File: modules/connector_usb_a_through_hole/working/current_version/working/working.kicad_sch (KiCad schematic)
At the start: 1 part, among them J1 scuath

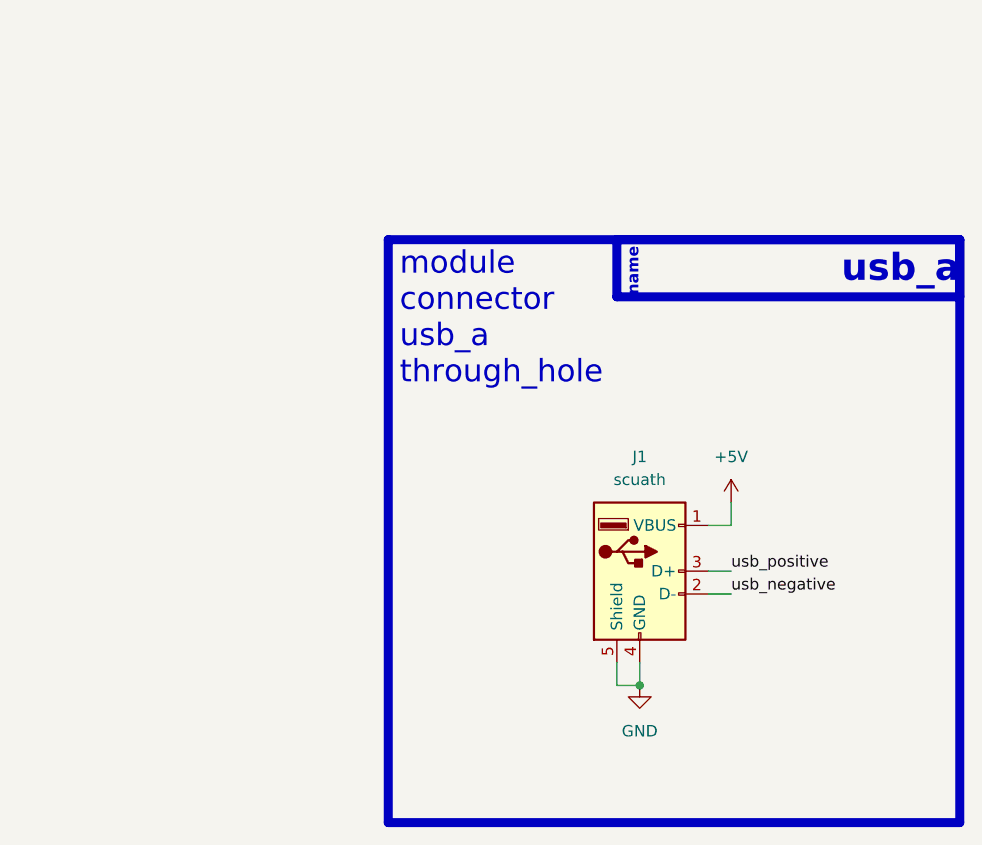
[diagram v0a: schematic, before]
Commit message: fixed formatting to be more consistent
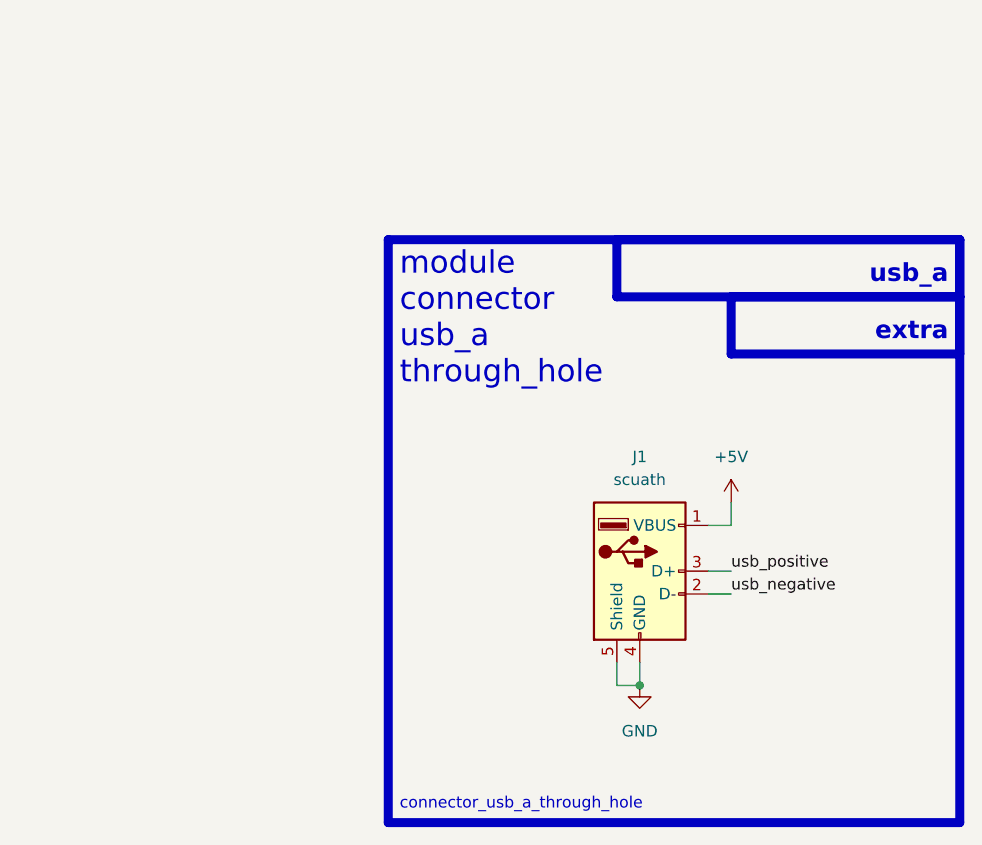
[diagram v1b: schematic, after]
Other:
- note added: "connector_usb_a_through_hole"
- note added: "extra"
- note removed: "name"
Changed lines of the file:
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@@
+    (fill (type none))
+  )
+  (rectangle (start 151.13 67.31) (end 176.53 73.66)
+    (stroke (width 1) (type default))
     (fill (type none))
   )
   (rectangle (start 138.43 60.96) (end 176.53 67.31)
     (stroke (width 1) (type default))
-    (fill (type color) (color 0 0 0 0))
+    (fill (type none))
   )
   (text "module\nconnector\nusb_a\nthrough_hole\n\n" (at 114.3 81.28 0)
     (effects (font (size 2.5 2.5)) (justify left bottom))
   )
-  (text "name" (at 140.97 67.31 90)
-    (effects (font (size 1.27 1.27) (thickness 0.254) bold (color 255 255 255 1)) (justify left bottom))
+  (text "connector_usb_a_through_hole" (at 114.3 124.46 0)
+    (effects (font (size 1.27 1.27)) (justify left bottom))
   )
-  (text "usb_a" (at 176.53 66.04 0)
-    (effects (font (size 3 3) (thickness 0.8) bold (color 255 255 255 1)) (justify right bottom))
+  (text "extra" (at 175.26 72.39 0)
+    (effects (font (size 2 2) (thickness 0.8) bold) (justify right bottom))
+  )
+  (text "usb_a" (at 175.26 66.04 0)
+    (effects (font (size 2 2) (thickness 0.8) bold) (justify right bottom))
   )
   (label "usb_positive" (at 151.13 97.79 0) (fields_autoplaced)

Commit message: a few fix ups
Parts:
- renumbered J1 to CON1
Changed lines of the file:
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@@
   (symbol (lib_id "oomlout_oomp_part_symbols:scuath_electronic_socket_usb_a_through_hole") (at 140.97 97.79 0) (unit 1)
     (in_bom yes) (on_board yes) (dnp no) (fields_autoplaced)
-    (property "Reference" "J1" (at 140.97 85.09 0)
+    (property "Reference" "CON1" (at 140.97 85.09 0)
       (effects (font (size 1.27 1.27)))
     )
@@
       (project "working"
         (path "/c9993764-076f-44f6-bf4c-6b69ce17c9e4"
-          (reference "J1") (unit 1)
+          (reference "CON1") (unit 1)
         )
       )

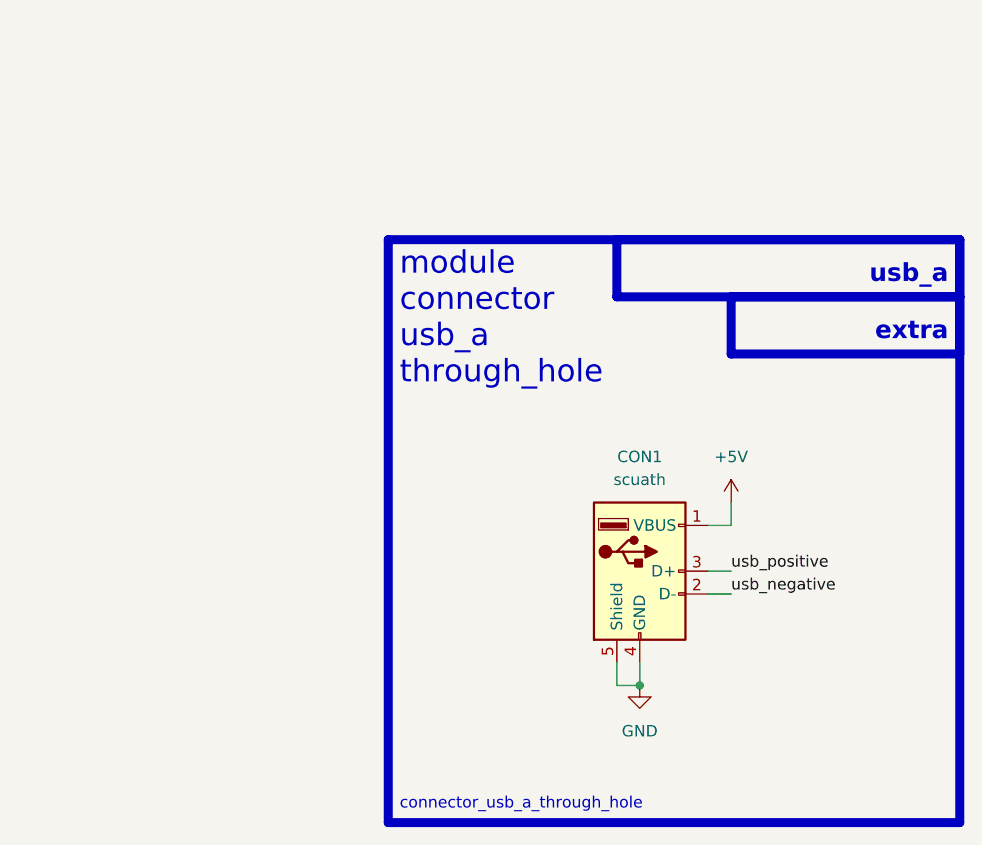
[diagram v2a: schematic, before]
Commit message: schematic formatting
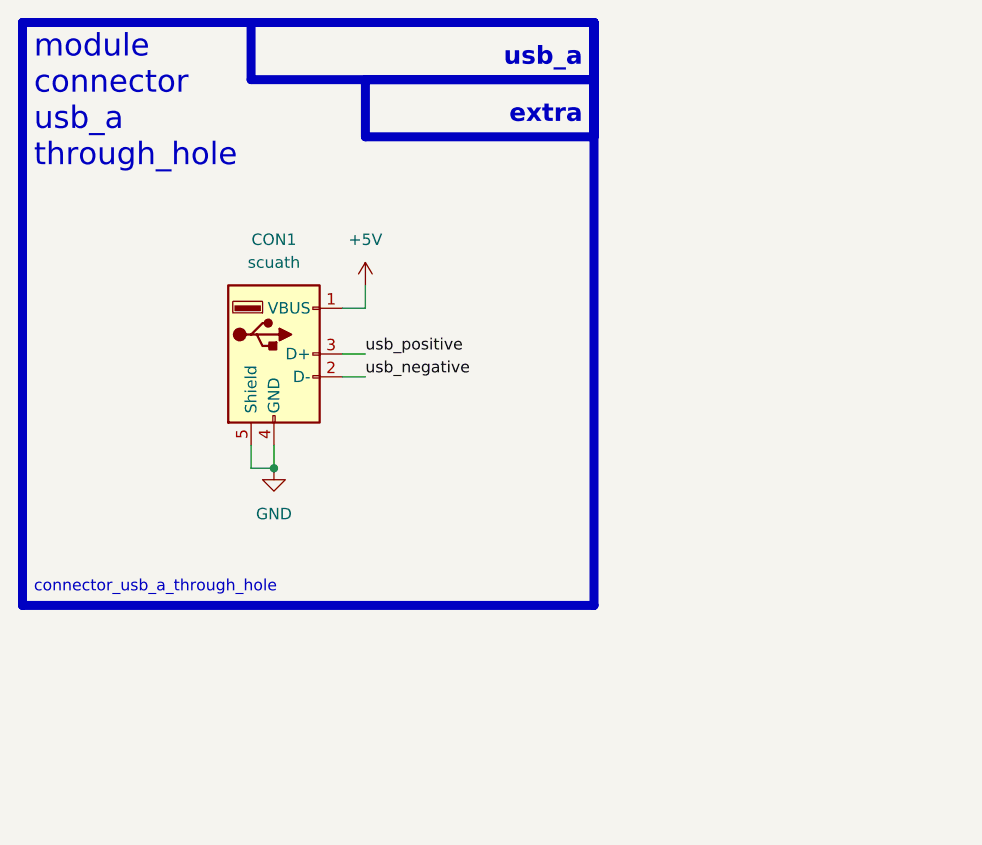
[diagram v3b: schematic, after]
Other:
- moved on the sheet: CON1
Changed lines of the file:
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@@
 (kicad_sch (version 20230121) (generator eeschema)
-  (paper "A4")
-  (junction (at 140.97 110.49) (diameter 0) (color 0 0 0 0)
+  (paper "A5")
+  (junction (at 100.33 86.36) (diameter 0) (color 0 0 0 0)
   )
-  (wire (pts (xy 148.59 97.79) (xy 151.13 97.79))
+  (wire (pts (xy 107.95 73.66) (xy 110.49 73.66))
     (stroke (width 0) (type default))
   )
-  (wire (pts (xy 138.43 107.95) (xy 138.43 110.49))
+  (wire (pts (xy 97.79 83.82) (xy 97.79 86.36))
     (stroke (width 0) (type default))
   )
-  (wire (pts (xy 151.13 90.17) (xy 151.13 92.71))
+  (wire (pts (xy 110.49 66.04) (xy 110.49 68.58))
     (stroke (width 0) (type default))
   )
-  (wire (pts (xy 148.59 92.71) (xy 151.13 92.71))
+  (wire (pts (xy 107.95 68.58) (xy 110.49 68.58))
     (stroke (width 0) (type default))
   )
-  (wire (pts (xy 140.97 107.95) (xy 140.97 110.49))
+  (wire (pts (xy 100.33 83.82) (xy 100.33 86.36))
     (stroke (width 0) (type default))
   )
-  (wire (pts (xy 138.43 110.49) (xy 140.97 110.49))
+  (wire (pts (xy 97.79 86.36) (xy 100.33 86.36))
     (stroke (width 0) (type default))
   )
-  (wire (pts (xy 148.59 100.33) (xy 151.13 100.33))
+  (wire (pts (xy 107.95 76.2) (xy 110.49 76.2))
     (stroke (width 0) (type default))
   )
-  (rectangle (start 113.03 60.96) (end 176.53 125.73)
+  (rectangle (start 72.39 36.83) (end 135.89 101.6)
     (stroke (width 1) (type default))
     (fill (type none))
   )
-  (rectangle (start 151.13 67.31) (end 176.53 73.66)
+  (rectangle (start 110.49 43.18) (end 135.89 49.53)
     (stroke (width 1) (type default))
     (fill (type none))
   )
-  (rectangle (start 138.43 60.96) (end 176.53 67.31)
+  (rectangle (start 97.79 36.83) (end 135.89 43.18)
     (stroke (width 1) (type default))
     (fill (type none))
   )
-  (text "module\nconnector\nusb_a\nthrough_hole\n\n" (at 114.3 81.28 0)
+  (text "module\nconnector\nusb_a\nthrough_hole\n\n" (at 73.66 57.15 0)
     (effects (font (size 2.5 2.5)) (justify left bottom))
   )
-  (text "connector_usb_a_through_hole" (at 114.3 124.46 0)
+  (text "connector_usb_a_through_hole" (at 73.66 100.33 0)
     (effects (font (size 1.27 1.27)) (justify left bottom))
   )
-  (text "extra" (at 175.26 72.39 0)
+  (text "extra" (at 134.62 48.26 0)
     (effects (font (size 2 2) (thickness 0.8) bold) (justify right bottom))
   )
-  (text "usb_a" (at 175.26 66.04 0)
+  (text "usb_a" (at 134.62 41.91 0)
     (effects (font (size 2 2) (thickness 0.8) bold) (justify right bottom))
   )
-  (label "usb_positive" (at 151.13 97.79 0) (fields_autoplaced)
+  (label "usb_positive" (at 110.49 73.66 0) (fields_autoplaced)
     (effects (font (size 1.27 1.27)) (justify left bottom))
   )
-  (label "usb_negative" (at 151.13 100.33 0) (fields_autoplaced)
+  (label "usb_negative" (at 110.49 76.2 0) (fields_autoplaced)
     (effects (font (size 1.27 1.27)) (justify left bottom))
   )
-  (symbol (lib_id "oomlout_oomp_part_symbols:scuath_electronic_socket_usb_a_through_hole") (at 140.97 97.79 0) (unit 1)
+  (symbol (lib_id "oomlout_oomp_part_symbols:scuath_electronic_socket_usb_a_through_hole") (at 100.33 73.66 0) (unit 1)
     (in_bom yes) (on_board yes) (dnp no) (fields_autoplaced)
-    (property "Reference" "CON1" (at 140.97 85.09 0)
+    (property "Reference" "CON1" (at 100.33 60.96 0)
       (effects (font (size 1.27 1.27)))
     )
-    (property "Value" "scuath" (at 140.97 87.63 0)
+    (property "Value" "scuath" (at 100.33 63.5 0)
       (effects (font (size 1.27 1.27)))
     )
-    (property "Footprint" "oomlout_oomp_part_footprints:scuath_electronic_socket_usb_a_through_hole" (at 144.78 99.06 0)
+    (property "Footprint" "oomlout_oomp_part_footprints:scuath_electronic_socket_usb_a_through_hole" (at 104.14 74.93 0)
       (effects (font (size 1.27 1.27)) hide)
     )
-    (property "Datasheet" "https://github.com/oomlout/oomlout_oomp_v3/parts/electronic_socket_usb_a_through_hole/datasheet.pdf" (at 144.78 99.06 0)
+    (property "Datasheet" "https://github.com/oomlout/oomlout_oomp_v3/parts/electronic_socket_usb_a_through_hole/datasheet.pdf" (at 104.14 74.93 0)
       (effects (font (size 1.27 1.27)) hide)
     )
@@
     )
   )
-  (symbol (lib_id "power:GND") (at 140.97 110.49 0) (unit 1)
+  (symbol (lib_id "power:GND") (at 100.33 86.36 0) (unit 1)
     (in_bom yes) (on_board yes) (dnp no) (fields_autoplaced)
-    (property "Reference" "#PWR012" (at 140.97 116.84 0)
+    (property "Reference" "#PWR012" (at 100.33 92.71 0)
       (effects (font (size 1.27 1.27)) hide)
     )
-    (property "Value" "GND" (at 140.97 115.57 0)
+    (property "Value" "GND" (at 100.33 91.44 0)
       (effects (font (size 1.27 1.27)))
     )
-    (property "Footprint" "" (at 140.97 110.49 0)
+    (property "Footprint" "" (at 100.33 86.36 0)
       (effects (font (size 1.27 1.27)) hide)
     )
-    (property "Datasheet" "" (at 140.97 110.49 0)
+    (property "Datasheet" "" (at 100.33 86.36 0)
       (effects (font (size 1.27 1.27)) hide)
     )
@@
     )
   )
-  (symbol (lib_id "power:+5V") (at 151.13 90.17 0) (unit 1)
+  (symbol (lib_id "power:+5V") (at 110.49 66.04 0) (unit 1)
     (in_bom yes) (on_board yes) (dnp no) (fields_autoplaced)
-    (property "Reference" "#PWR013" (at 151.13 93.98 0)
+    (property "Reference" "#PWR013" (at 110.49 69.85 0)
       (effects (font (size 1.27 1.27)) hide)
     )
-    (property "Value" "+5V" (at 151.13 85.09 0)
+    (property "Value" "+5V" (at 110.49 60.96 0)
       (effects (font (size 1.27 1.27)))
     )
-    (property "Footprint" "" (at 151.13 90.17 0)
+    (property "Footprint" "" (at 110.49 66.04 0)
       (effects (font (size 1.27 1.27)) hide)
     )
-    (property "Datasheet" "" (at 151.13 90.17 0)
+    (property "Datasheet" "" (at 110.49 66.04 0)
       (effects (font (size 1.27 1.27)) hide)
     )
